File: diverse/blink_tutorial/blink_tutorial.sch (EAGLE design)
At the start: 12 parts, among them T1 BC547, T2 BC547

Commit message: updated wemos and diverse boards
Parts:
- U$1: value (none) -> SIG1
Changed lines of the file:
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@@
 <?xml version="1.0" encoding="utf-8"?>
 <!DOCTYPE eagle SYSTEM "eagle.dtd">
-<eagle version="9.3.0">
+<eagle version="9.6.2">
 <drawing>
 <settings>
@@
 <part name="JP1" library="pinhead" library_urn="urn:adsk.eagle:library:325" deviceset="PINHD-1X2" device="" package3d_urn="urn:adsk.eagle:package:22435/2"/>
 <part name="GND1" library="supply1" library_urn="urn:adsk.eagle:library:371" deviceset="GND" device=""/>
-<part name="U$1" library="SWI_COMMONS" deviceset="BRAND_SWI" device="5X7"/>
+<part name="U$1" library="SWI_COMMONS" deviceset="BRAND_SWI" device="5X7" value="SIG1"/>
 </parts>
 <sheets>
@@
 </sheet>
 </sheets>
+<errors>
+</errors>
 </schematic>
 </drawing>

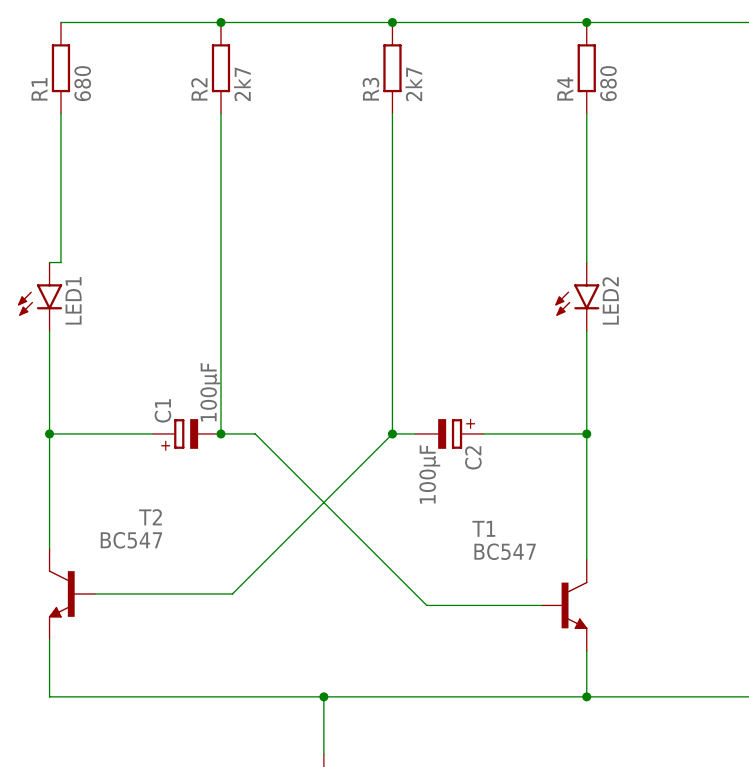
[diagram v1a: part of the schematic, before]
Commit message: changed resistor footprint to 1206
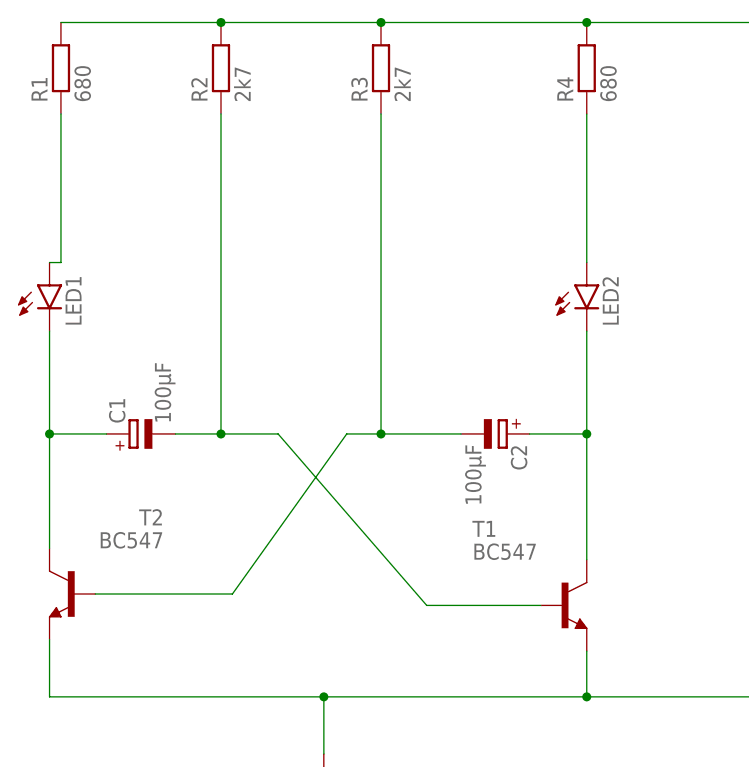
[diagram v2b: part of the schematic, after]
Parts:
- R1, R2, R3, R4: device rcl:R-EU_R0805 -> SWI_COMMONS:R-EU_M1206
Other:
- moved on the sheet: C1, C2, R3
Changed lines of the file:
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@@
 <parts>
 <part name="FRAME1" library="SWI_COMMONS" deviceset="A4L-LOC" device=""/>
-<part name="R1" library="rcl" library_urn="urn:adsk.eagle:library:334" deviceset="R-EU_" device="R0805" package3d_urn="urn:adsk.eagle:package:23553/2" value="680"/>
-<part name="R2" library="rcl" library_urn="urn:adsk.eagle:library:334" deviceset="R-EU_" device="R0805" package3d_urn="urn:adsk.eagle:package:23553/2" value="2k7"/>
-<part name="R3" library="rcl" library_urn="urn:adsk.eagle:library:334" deviceset="R-EU_" device="R0805" package3d_urn="urn:adsk.eagle:package:23553/2" value="2k7"/>
-<part name="R4" library="rcl" library_urn="urn:adsk.eagle:library:334" deviceset="R-EU_" device="R0805" package3d_urn="urn:adsk.eagle:package:23553/2" value="680"/>
 <part name="LED1" library="led" library_urn="urn:adsk.eagle:library:259" deviceset="LED" device="5MM" package3d_urn="urn:adsk.eagle:package:15799/2"/>
 <part name="LED2" library="led" library_urn="urn:adsk.eagle:library:259" deviceset="LED" device="5MM" package3d_urn="urn:adsk.eagle:package:15799/2"/>
@@
 <part name="GND1" library="supply1" library_urn="urn:adsk.eagle:library:371" deviceset="GND" device=""/>
 <part name="U$1" library="SWI_COMMONS" deviceset="BRAND_SWI" device="5X7" value="SIG1"/>
+<part name="R1" library="SWI_COMMONS" deviceset="R-EU_" device="M1206" value="680"/>
+<part name="R2" library="SWI_COMMONS" deviceset="R-EU_" device="M1206" value="2k7"/>
+<part name="R3" library="SWI_COMMONS" deviceset="R-EU_" device="M1206" value="2k7"/>
+<part name="R4" library="SWI_COMMONS" deviceset="R-EU_" device="M1206" value="680"/>
 </parts>
 <sheets>
@@
 <attribute name="SHEET" x="220.345" y="-7.62" size="2.54" layer="94"/>
 </instance>
-<instance part="R1" gate="G$1" x="35.56" y="121.92" smashed="yes" rot="R90">
-<attribute name="NAME" x="34.0614" y="118.11" size="1.778" layer="95" rot="R90"/>
-<attribute name="VALUE" x="38.862" y="118.11" size="1.778" layer="96" rot="R90"/>
-</instance>
-<instance part="R2" gate="G$1" x="53.34" y="121.92" smashed="yes" rot="R90">
-<attribute name="NAME" x="51.8414" y="118.11" size="1.778" layer="95" rot="R90"/>
-<attribute name="VALUE" x="56.642" y="118.11" size="1.778" layer="96" rot="R90"/>
-</instance>
-<instance part="R3" gate="G$1" x="72.39" y="121.92" smashed="yes" rot="R90">
-<attribute name="NAME" x="70.8914" y="118.11" size="1.778" layer="95" rot="R90"/>
-<attribute name="VALUE" x="75.692" y="118.11" size="1.778" layer="96" rot="R90"/>
-</instance>
-<instance part="R4" gate="G$1" x="93.98" y="121.92" smashed="yes" rot="R90">
-<attribute name="NAME" x="92.4814" y="118.11" size="1.778" layer="95" rot="R90"/>
-<attribute name="VALUE" x="97.282" y="118.11" size="1.778" layer="96" rot="R90"/>
-</instance>
 <instance part="LED1" gate="G$1" x="34.29" y="97.79" smashed="yes">
 <attribute name="NAME" x="37.846" y="93.218" size="1.778" layer="95" rot="R90"/>
@@
 <attribute name="VALUE" x="99.695" y="93.218" size="1.778" layer="96" rot="R90"/>
 </instance>
-<instance part="C1" gate="G$1" x="48.26" y="81.28" smashed="yes" rot="R90">
-<attribute name="NAME" x="47.7774" y="82.423" size="1.778" layer="95" rot="R90"/>
-<attribute name="VALUE" x="52.8574" y="82.423" size="1.778" layer="96" rot="R90"/>
+<instance part="C1" gate="G$1" x="43.18" y="81.28" smashed="yes" rot="R90">
+<attribute name="NAME" x="42.6974" y="82.423" size="1.778" layer="95" rot="R90"/>
+<attribute name="VALUE" x="47.7774" y="82.423" size="1.778" layer="96" rot="R90"/>
 </instance>
-<instance part="C2" gate="G$1" x="80.01" y="81.28" smashed="yes" rot="R270">
-<attribute name="NAME" x="80.4926" y="80.137" size="1.778" layer="95" rot="R270"/>
-<attribute name="VALUE" x="75.4126" y="80.137" size="1.778" layer="96" rot="R270"/>
+<instance part="C2" gate="G$1" x="85.09" y="81.28" smashed="yes" rot="R270">
+<attribute name="NAME" x="85.5726" y="80.137" size="1.778" layer="95" rot="R270"/>
+<attribute name="VALUE" x="80.4926" y="80.137" size="1.778" layer="96" rot="R270"/>
 </instance>
 <instance part="T1" gate="G$1" x="91.44" y="62.23" smashed="yes">
@@
 </instance>
 <instance part="U$1" gate="G$1" x="152.4" y="15.24" smashed="yes"/>
+<instance part="R1" gate="G$1" x="35.56" y="121.92" smashed="yes" rot="R90">
+<attribute name="NAME" x="34.0614" y="118.11" size="1.778" layer="95" rot="R90"/>
+<attribute name="VALUE" x="38.862" y="118.11" size="1.778" layer="96" rot="R90"/>
+</instance>
+<instance part="R2" gate="G$1" x="53.34" y="121.92" smashed="yes" rot="R90">
+<attribute name="NAME" x="51.8414" y="118.11" size="1.778" layer="95" rot="R90"/>
+<attribute name="VALUE" x="56.642" y="118.11" size="1.778" layer="96" rot="R90"/>
+</instance>
+<instance part="R3" gate="G$1" x="71.12" y="121.92" smashed="yes" rot="R90">
+<attribute name="NAME" x="69.6214" y="118.11" size="1.778" layer="95" rot="R90"/>
+<attribute name="VALUE" x="74.422" y="118.11" size="1.778" layer="96" rot="R90"/>
+</instance>
+<instance part="R4" gate="G$1" x="93.98" y="121.92" smashed="yes" rot="R90">
+<attribute name="NAME" x="92.4814" y="118.11" size="1.778" layer="95" rot="R90"/>
+<attribute name="VALUE" x="97.282" y="118.11" size="1.778" layer="96" rot="R90"/>
+</instance>
 </instances>
 <busses>
@@
 <wire x1="127" y1="96.52" x2="116.84" y2="96.52" width="0.1524" layer="91"/>
 <wire x1="116.84" y1="96.52" x2="116.84" y2="127" width="0.1524" layer="91"/>
-<pinref part="R4" gate="G$1" pin="2"/>
 <wire x1="116.84" y1="127" x2="93.98" y2="127" width="0.1524" layer="91"/>
-<pinref part="R3" gate="G$1" pin="2"/>
-<wire x1="93.98" y1="127" x2="72.39" y2="127" width="0.1524" layer="91"/>
-<junction x="93.98" y="127"/>
+<pinref part="R1" gate="G$1" pin="2"/>
 <pinref part="R2" gate="G$1" pin="2"/>
-<wire x1="72.39" y1="127" x2="53.34" y2="127" width="0.1524" layer="91"/>
-<junction x="72.39" y="127"/>
-<pinref part="R1" gate="G$1" pin="2"/>
+<wire x1="93.98" y1="127" x2="71.12" y2="127" width="0.1524" layer="91"/>
+<wire x1="71.12" y1="127" x2="53.34" y2="127" width="0.1524" layer="91"/>
 <wire x1="53.34" y1="127" x2="35.56" y2="127" width="0.1524" layer="91"/>
 <junction x="53.34" y="127"/>
+<pinref part="R3" gate="G$1" pin="2"/>
+<junction x="71.12" y="127"/>
+<pinref part="R4" gate="G$1" pin="2"/>
+<junction x="93.98" y="127"/>
 </segment>
 </net>
 <net name="N$2" class="0">
 <segment>
-<pinref part="R1" gate="G$1" pin="1"/>
 <pinref part="LED1" gate="G$1" pin="A"/>
 <wire x1="35.56" y1="116.84" x2="35.56" y2="100.33" width="0.1524" layer="91"/>
 <wire x1="35.56" y1="100.33" x2="34.29" y2="100.33" width="0.1524" layer="91"/>
+<pinref part="R1" gate="G$1" pin="1"/>
 </segment>
 </net>
 <net name="N$3" class="0">
 <segment>
-<pinref part="R4" gate="G$1" pin="1"/>
 <pinref part="LED2" gate="G$1" pin="A"/>
 <wire x1="93.98" y1="116.84" x2="93.98" y2="100.33" width="0.1524" layer="91"/>
+<pinref part="R4" gate="G$1" pin="1"/>
 </segment>
 </net>
@@
 <pinref part="C1" gate="G$1" pin="+"/>
 <wire x1="34.29" y1="81.28" x2="34.29" y2="68.58" width="0.1524" layer="91"/>
-<wire x1="45.72" y1="81.28" x2="34.29" y2="81.28" width="0.1524" layer="91"/>
+<wire x1="40.64" y1="81.28" x2="34.29" y2="81.28" width="0.1524" layer="91"/>
 <junction x="34.29" y="81.28"/>
 </segment>
@@
 <pinref part="C2" gate="G$1" pin="+"/>
 <wire x1="93.98" y1="81.28" x2="93.98" y2="67.31" width="0.1524" layer="91"/>
-<wire x1="82.55" y1="81.28" x2="93.98" y2="81.28" width="0.1524" layer="91"/>
+<wire x1="87.63" y1="81.28" x2="93.98" y2="81.28" width="0.1524" layer="91"/>
 <junction x="93.98" y="81.28"/>
 </segment>
@@
 <net name="N$6" class="0">
 <segment>
+<pinref part="C2" gate="G$1" pin="-"/>
+<wire x1="67.31" y1="81.28" x2="71.12" y2="81.28" width="0.1524" layer="91"/>
+<pinref part="T2" gate="G$1" pin="B"/>
+<wire x1="71.12" y1="81.28" x2="80.01" y2="81.28" width="0.1524" layer="91"/>
+<wire x1="67.31" y1="81.28" x2="54.61" y2="63.5" width="0.1524" layer="91"/>
+<wire x1="54.61" y1="63.5" x2="39.37" y2="63.5" width="0.1524" layer="91"/>
 <pinref part="R3" gate="G$1" pin="1"/>
-<pinref part="C2" gate="G$1" pin="-"/>
-<wire x1="72.39" y1="116.84" x2="72.39" y2="81.28" width="0.1524" layer="91"/>
-<wire x1="72.39" y1="81.28" x2="74.93" y2="81.28" width="0.1524" layer="91"/>
-<pinref part="T2" gate="G$1" pin="B"/>
-<wire x1="72.39" y1="81.28" x2="54.61" y2="63.5" width="0.1524" layer="91"/>
-<wire x1="54.61" y1="63.5" x2="39.37" y2="63.5" width="0.1524" layer="91"/>
-<junction x="72.39" y="81.28"/>
+<wire x1="71.12" y1="116.84" x2="71.12" y2="81.28" width="0.1524" layer="91"/>
+<junction x="71.12" y="81.28"/>
 </segment>
 </net>
 <net name="N$7" class="0">
 <segment>
-<pinref part="R2" gate="G$1" pin="1"/>
 <pinref part="C1" gate="G$1" pin="-"/>
-<wire x1="53.34" y1="116.84" x2="53.34" y2="81.28" width="0.1524" layer="91"/>
-<wire x1="53.34" y1="81.28" x2="57.15" y2="81.28" width="0.1524" layer="91"/>
-<wire x1="57.15" y1="81.28" x2="76.2" y2="62.23" width="0.1524" layer="91"/>
-<junction x="53.34" y="81.28"/>
+<wire x1="48.26" y1="81.28" x2="53.34" y2="81.28" width="0.1524" layer="91"/>
+<wire x1="53.34" y1="81.28" x2="59.69" y2="81.28" width="0.1524" layer="91"/>
+<wire x1="59.69" y1="81.28" x2="76.2" y2="62.23" width="0.1524" layer="91"/>
 <pinref part="T1" gate="G$1" pin="B"/>
 <wire x1="76.2" y1="62.23" x2="88.9" y2="62.23" width="0.1524" layer="91"/>
+<pinref part="R2" gate="G$1" pin="1"/>
+<wire x1="53.34" y1="116.84" x2="53.34" y2="81.28" width="0.1524" layer="91"/>
+<junction x="53.34" y="81.28"/>
 </segment>
 </net>
